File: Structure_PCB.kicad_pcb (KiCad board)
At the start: 2 copper layers, 180 x 100 mm, 101 parts, among them J10 JST-GH 4Pin, J11 JST-GH 4Pin, J12 JST-GH 4Pin, J6 6620XX236022_662004236022, J9 Conn_02x04_Top_Bottom, K2 FINDER-30.22

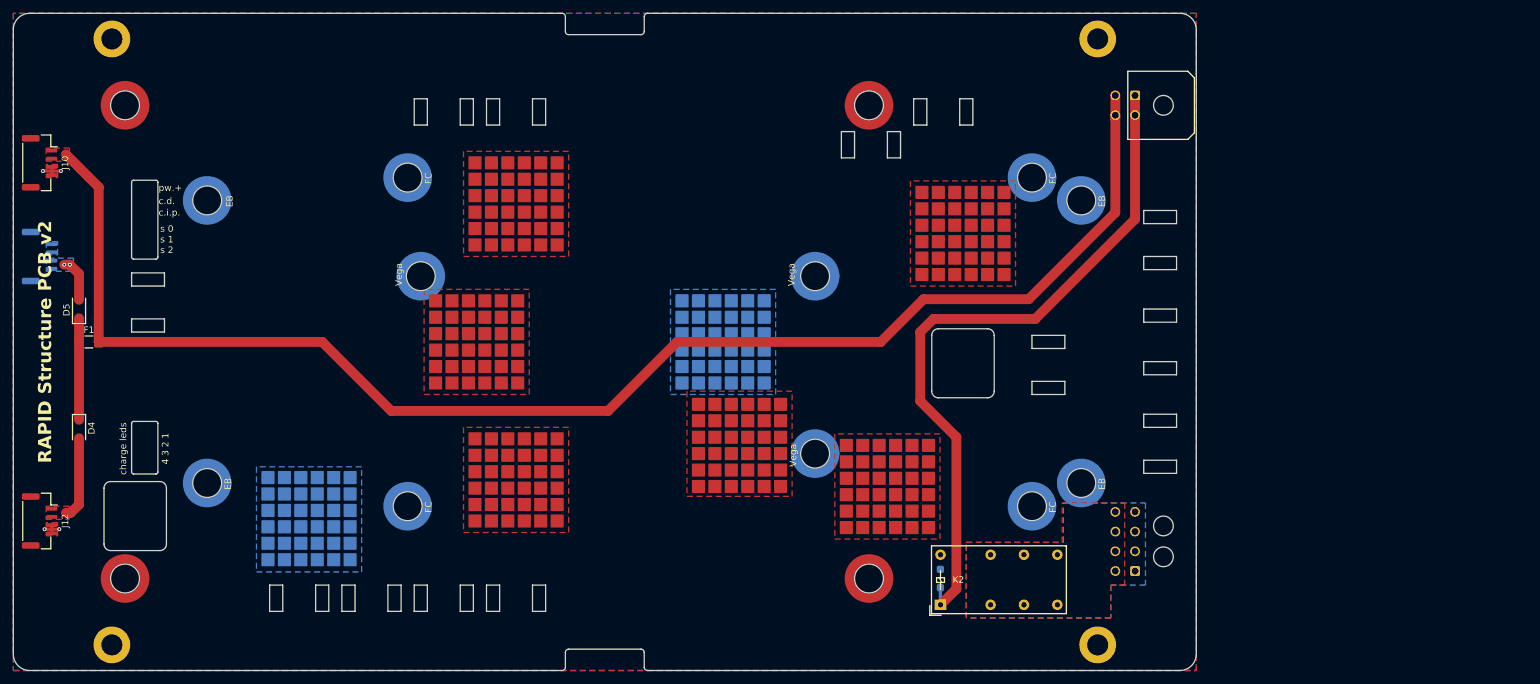
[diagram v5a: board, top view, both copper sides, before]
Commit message: added some thermal pads
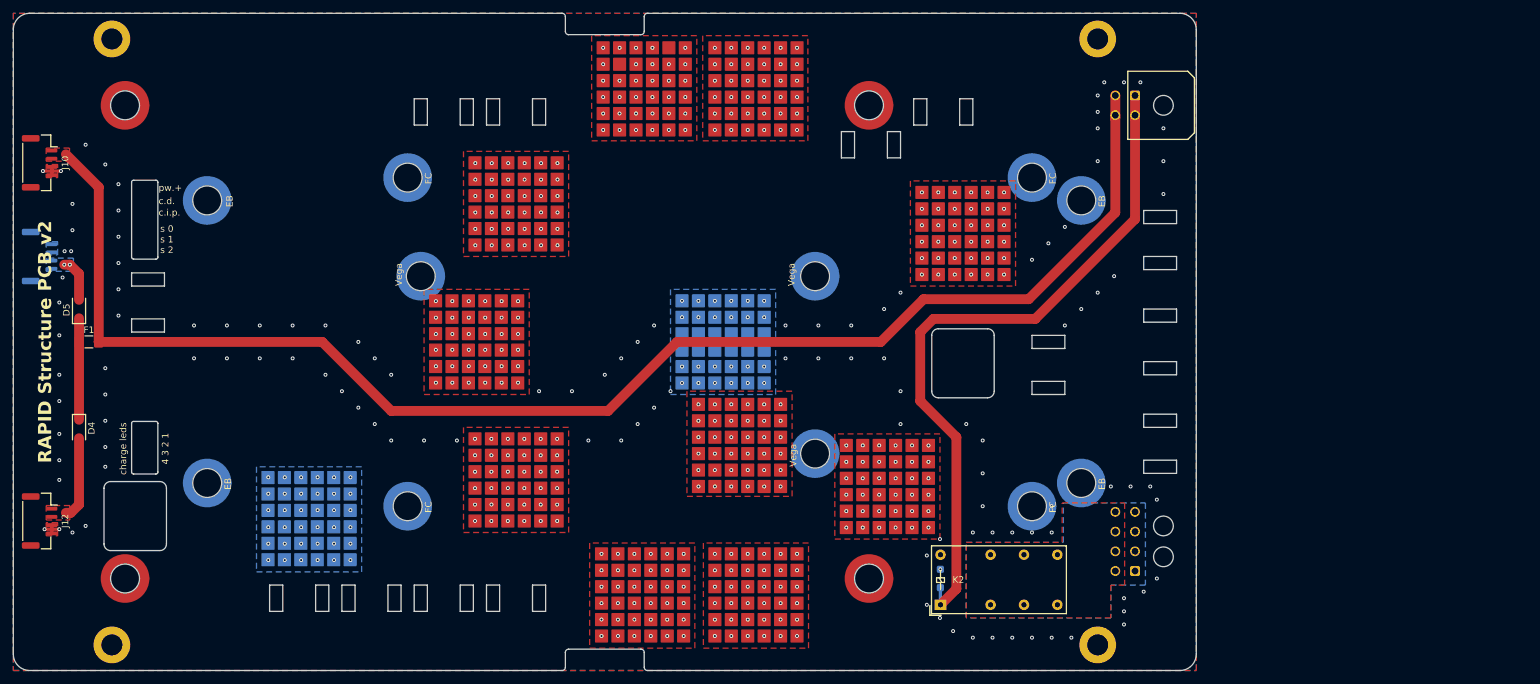
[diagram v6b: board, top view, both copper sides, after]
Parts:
- added HS100: Heatsink_Pad, Heatsink:würth 5x5 heat pads, F.Cu at (150.8, 138.5)
- added HS101: Heatsink_Pad, Heatsink:würth 5x5 heat pads, F.Cu at (168.0, 66.5)
- added HS102: Heatsink_Pad, Heatsink:würth 5x5 heat pads, F.Cu at (150.8, 143.5)
- added HS103: Heatsink_Pad, Heatsink:würth 5x5 heat pads, F.Cu at (141.0, 56.5)
- added HS104: Heatsink_Pad, Heatsink:würth 5x5 heat pads, F.Cu at (158.0, 133.5)
- added HS105: Heatsink_Pad, Heatsink:würth 5x5 heat pads, F.Cu at (141.0, 61.5)
- added HS106: Heatsink_Pad, Heatsink:würth 5x5 heat pads, F.Cu at (158.0, 138.5)
- added HS107: Heatsink_Pad, Heatsink:würth 5x5 heat pads, F.Cu at (141.0, 66.5)
- added HS108: Heatsink_Pad, Heatsink:würth 5x5 heat pads, F.Cu at (158.0, 143.5)
- added HS109: Heatsink_Pad, Heatsink:würth 5x5 heat pads, F.Cu at (146.0, 56.5)
- added HS110: Heatsink_Pad, Heatsink:würth 5x5 heat pads, F.Cu at (163.0, 133.5)
- added HS111: Heatsink_Pad, Heatsink:würth 5x5 heat pads, F.Cu at (146.0, 61.5)
- added HS112: Heatsink_Pad, Heatsink:würth 5x5 heat pads, F.Cu at (163.0, 138.5)
- added HS113: Heatsink_Pad, Heatsink:würth 5x5 heat pads, F.Cu at (146.0, 66.5)
- added HS114: Heatsink_Pad, Heatsink:würth 5x5 heat pads, F.Cu at (163.0, 143.5)
- added HS115: Heatsink_Pad, Heatsink:würth 5x5 heat pads, F.Cu at (151.0, 56.5)
- added HS116: Heatsink_Pad, Heatsink:würth 5x5 heat pads, F.Cu at (168.0, 133.5)
- added HS117: Heatsink_Pad, Heatsink:würth 5x5 heat pads, F.Cu at (151.0, 61.5)
- added HS118: Heatsink_Pad, Heatsink:würth 5x5 heat pads, F.Cu at (168.0, 138.5)
- added HS119: Heatsink_Pad, Heatsink:würth 5x5 heat pads, F.Cu at (151.0, 66.5)
- added HS120: Heatsink_Pad, Heatsink:würth 5x5 heat pads, F.Cu at (168.0, 143.5)
- added HS85: Heatsink_Pad, Heatsink:würth 5x5 heat pads, F.Cu at (158.0, 56.5)
- added HS86: Heatsink_Pad, Heatsink:würth 5x5 heat pads, F.Cu at (140.8, 133.5)
- added HS87: Heatsink_Pad, Heatsink:würth 5x5 heat pads, F.Cu at (158.0, 61.5)
- added HS88: Heatsink_Pad, Heatsink:würth 5x5 heat pads, F.Cu at (140.8, 138.5)
- added HS89: Heatsink_Pad, Heatsink:würth 5x5 heat pads, F.Cu at (158.0, 66.5)
- added HS90: Heatsink_Pad, Heatsink:würth 5x5 heat pads, F.Cu at (140.8, 143.5)
- added HS91: Heatsink_Pad, Heatsink:würth 5x5 heat pads, F.Cu at (163.0, 56.5)
- added HS92: Heatsink_Pad, Heatsink:würth 5x5 heat pads, F.Cu at (145.8, 133.5)
- added HS93: Heatsink_Pad, Heatsink:würth 5x5 heat pads, F.Cu at (163.0, 61.5)
- added HS94: Heatsink_Pad, Heatsink:würth 5x5 heat pads, F.Cu at (145.8, 138.5)
- added HS95: Heatsink_Pad, Heatsink:würth 5x5 heat pads, F.Cu at (163.0, 66.5)
- added HS96: Heatsink_Pad, Heatsink:würth 5x5 heat pads, F.Cu at (145.8, 143.5)
- added HS97: Heatsink_Pad, Heatsink:würth 5x5 heat pads, F.Cu at (168.0, 56.5)
- added HS98: Heatsink_Pad, Heatsink:würth 5x5 heat pads, F.Cu at (150.8, 133.5)
- added HS99: Heatsink_Pad, Heatsink:würth 5x5 heat pads, F.Cu at (168.0, 61.5)
- H1, H10, H11, H12, H13, H14, H15, H16, H17, H18, H19, H2, H3, H4, H5, H6, H7, H8, H9: value MountingHole -> MountingHole_Pad
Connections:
- H1 pad 1: (no net) -> GND
- H10 pad 1: (no net) -> GND
- H11 pad 1: (no net) -> GND
- H12 pad 1: (no net) -> GND
- H13 pad 1: (no net) -> GND
- H14 pad 1: (no net) -> GND
- H15 pad 1: (no net) -> GND
- H16 pad 1: (no net) -> GND
- H17 pad 1: (no net) -> GND
- H18 pad 1: (no net) -> GND
- H19 pad 1: (no net) -> GND
- H2 pad 1: (no net) -> GND
- H3 pad 1: (no net) -> GND
- H4 pad 1: (no net) -> GND
- H5 pad 1: (no net) -> GND
- H6 pad 1: (no net) -> GND
- H7 pad 1: (no net) -> GND
- H8 pad 1: (no net) -> GND
- H9 pad 1: (no net) -> GND
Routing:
- net GND: vias 4 -> 538

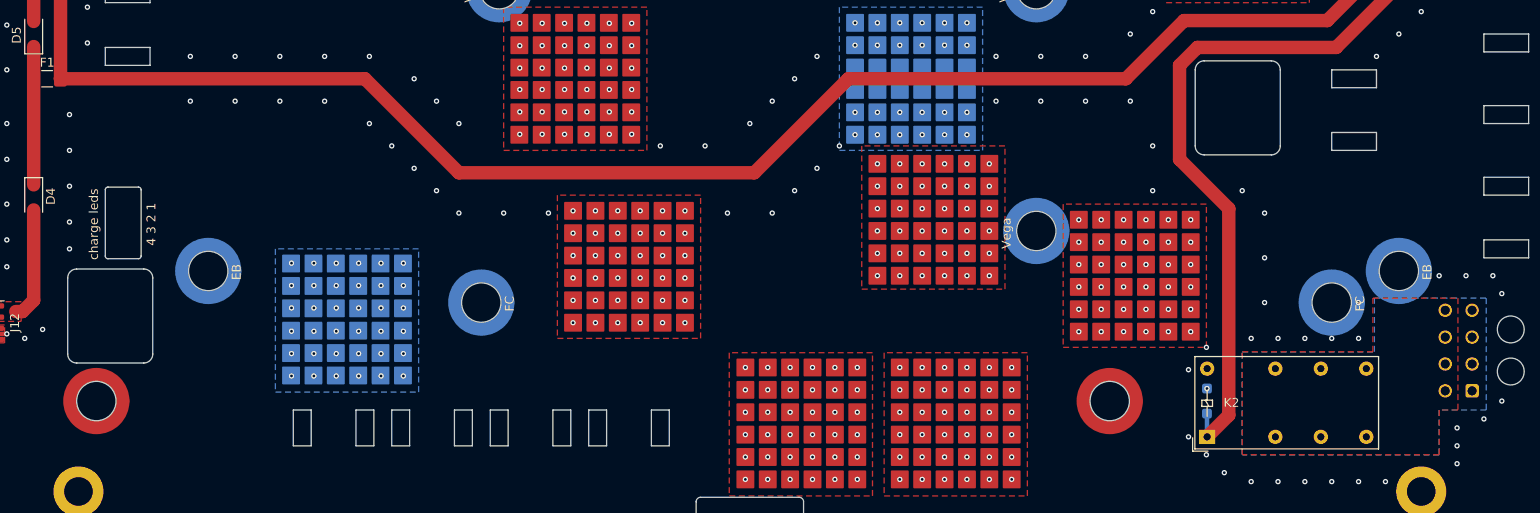
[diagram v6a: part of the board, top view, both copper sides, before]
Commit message: Fix relay footprint, correct zones, round off through trace
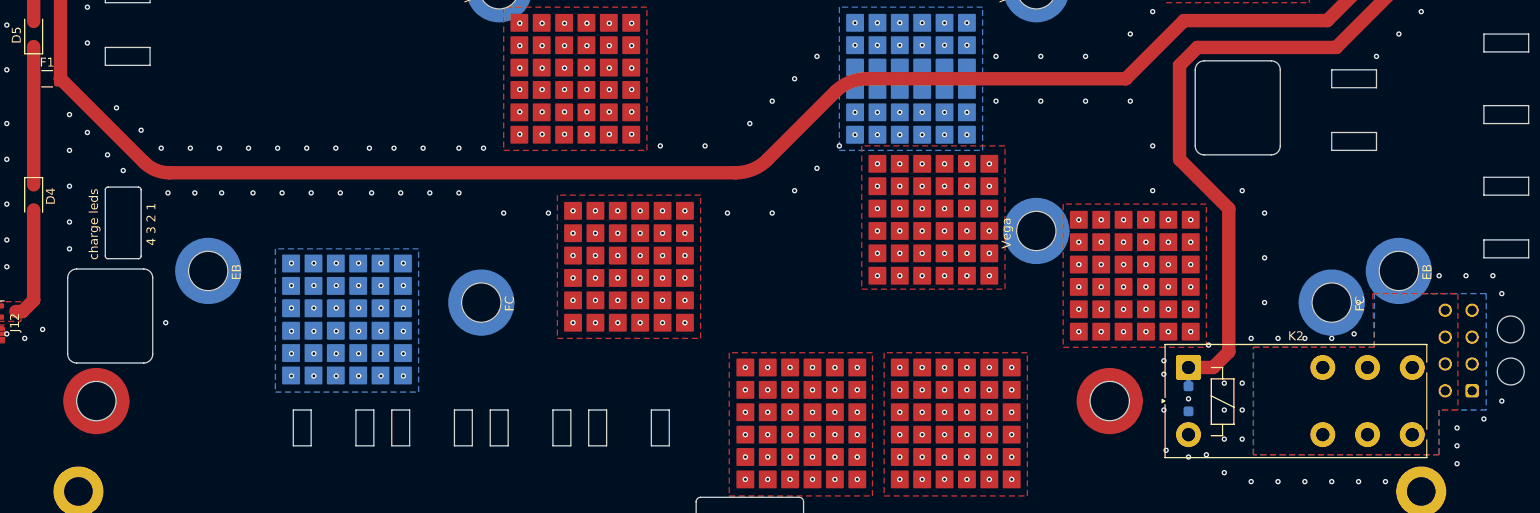
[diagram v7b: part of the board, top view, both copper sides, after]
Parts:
- K2: value FINDER-30.22 -> FINDER-40.61; footprint Relay_THT:Relay_DPDT_Finder_30.22 -> Relay_THT:Relay_SPDT_Finder_40.61
- moved K2 8.02 mm to (189.0, 132.2)
- moved D6 2.08 mm to (189.0, 135.8), turned to -90 degrees
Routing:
- net /post_arm: track 106.5 -> 100.7 mm
- net /SBout: track 220.5 -> 219.8 mm
- net GND: vias 538 -> 559

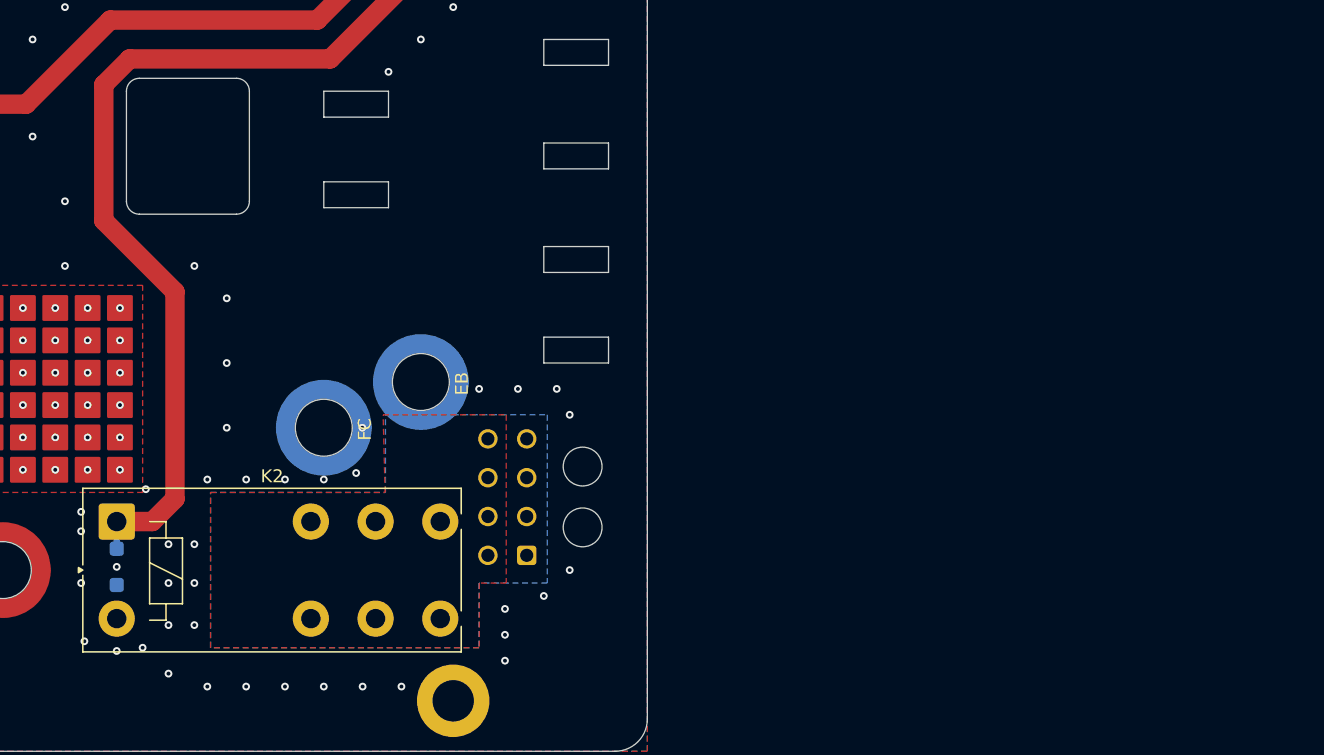
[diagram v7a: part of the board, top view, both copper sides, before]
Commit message: Increase distance between relais and fc
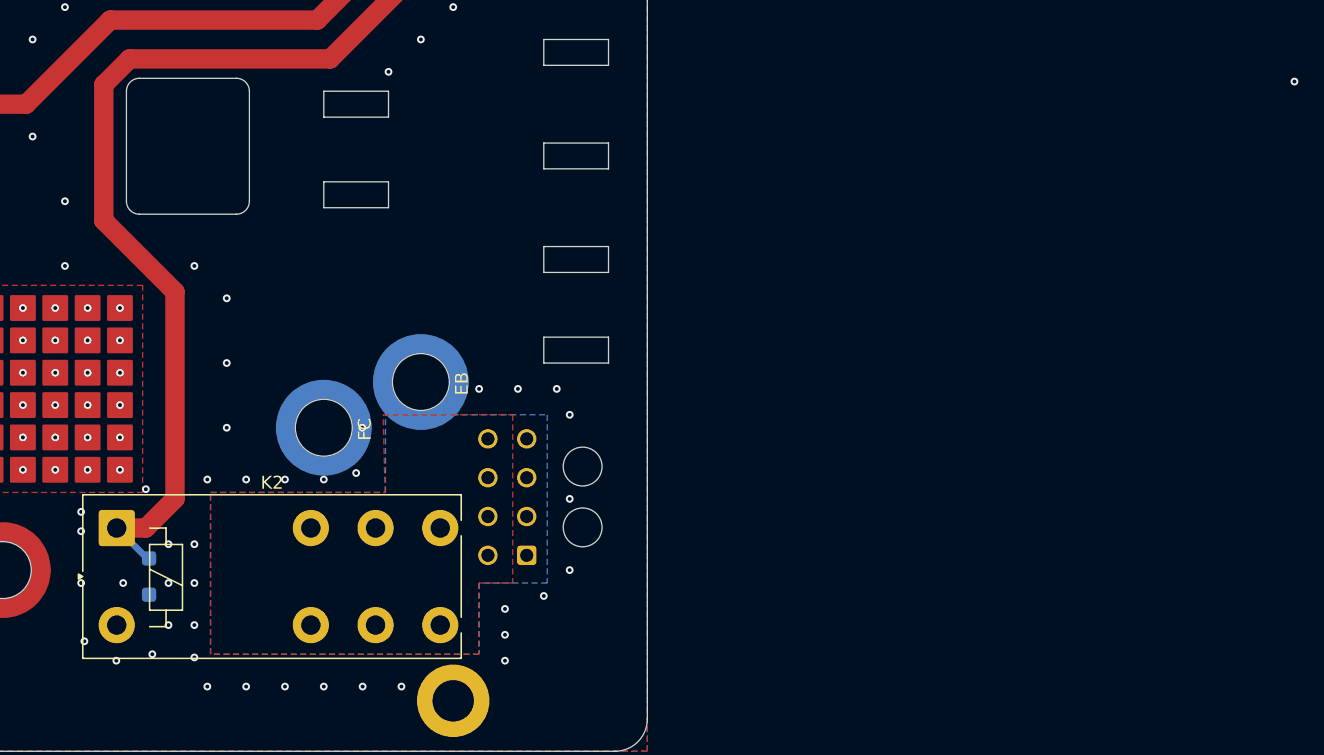
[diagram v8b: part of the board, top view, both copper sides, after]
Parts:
- moved D6 2.61 mm to (191.5, 136.5)
- moved K2 0.50 mm to (189.0, 132.8)
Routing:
- net /post_arm: track 100.7 -> 102.3 mm
- net GND: vias 559 -> 560
- net (no net): vias 0 -> 1
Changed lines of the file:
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@@
 	(footprint "Relay_THT:Relay_SPDT_Finder_40.61"
 		(layer "F.Cu")
-		(at 189 132.25)
+		(at 189 132.75)
 		(descr "SPDT relay, Finder 40.61, 16A, 250V, body size 29x12.4mm, height 25mm, pitch 5x7.5mm, https://cdn.findernet.com/app/uploads/S40EN.pdf")
 		(tags "2-Form-C")
@@
 	(footprint "Diode_SMD:D_SOD-123F"
 		(layer "B.Cu")
-		(at 189 135.75 -90)
+		(at 191.5 136.5 -90)
 		(descr "D_SOD-123F")
 		(tags "D_SOD-123F")
@@
 	)
 	(gr_text "PB power in"
-		(at 57.2 80 90)
+		(at 61 87 270)
 		(layer "B.Paste")
 		(effects
@@
 				(thickness 0.2)
 			)
-			(justify top)
+			(justify top mirror)
 		)
 	)
@@
 		)
 	)
+	(via
+		(at 280 98.25)
+		(size 0.6)
+		(drill 0.3)
+		(layers "F.Cu" "B.Cu")
+		(net 0)
+	)
 	(segment
 		(start 55.85 74)
@@
 	)
 	(via
-		(at 189 142.25)
+		(at 188.96785 143)
 		(size 0.6)
 		(drill 0.3)
@@
 	)
 	(via
-		(at 193 144)
+		(at 191.75 142.5)
 		(size 0.6)
 		(drill 0.3)
@@
 	)
 	(via
+		(at 224 130.5)
+		(size 0.6)
+		(drill 0.3)
+		(layers "F.Cu" "B.Cu")
+		(free yes)
+		(net 1)
+	)
+	(via
 		(at 124.3 93.8)
 		(size 0.6)
@@
 	)
 	(via
-		(at 191 142)
+		(at 195 142.75)
 		(size 0.6)
 		(drill 0.3)
@@
 	)
 	(via
-		(at 189 135.75)
+		(at 189.5 137)
 		(size 0.6)
 		(drill 0.3)
@@
 	)
 	(segment
-		(start 205.5 96.5)
-		(end 190 96.5)
+		(start 220.68 66)
+		(end 220.68 62.5)
 		(width 1.5)
 		(layer "F.Cu")
@@
 	)
 	(segment
-		(start 220.68 66)
-		(end 220.68 62.5)
+		(start 190 96.5)
+		(end 188 98.5)
 		(width 1.5)
 		(layer "F.Cu")
@@
 	)
 	(segment
-		(start 220.68 81.32)
-		(end 205.5 96.5)
+		(start 188 109)
+		(end 193.5 114.5)
 		(width 1.5)
 		(layer "F.Cu")
@@
 	)
 	(segment
-		(start 193.5 114.5)
-		(end 193.5 130.5)
+		(start 191.25 132.75)
+		(end 189 132.75)
 		(width 1.5)
 		(layer "F.Cu")
@@
 	)
 	(segment
-		(start 220.68 66)
-		(end 220.68 81.32)
+		(start 220.68 65.5)
+		(end 220.68 66)
 		(width 1.5)
 		(layer "F.Cu")
@@
 	)
 	(segment
-		(start 188 98.5)
-		(end 188 109)
+		(start 220.68 66)
+		(end 220.68 81.32)
 		(width 1.5)
 		(layer "F.Cu")
@@
 	)
 	(segment
-		(start 188 109)
-		(end 193.5 114.5)
+		(start 205.5 96.5)
+		(end 190 96.5)
 		(width 1.5)
 		(layer "F.Cu")
@@
 	)
 	(segment
-		(start 220.68 65.5)
-		(end 220.68 66)
+		(start 193.5 114.5)
+		(end 193.5 130.5)
 		(width 1.5)
 		(layer "F.Cu")
@@
 	)
 	(segment
-		(start 191.75 132.25)
-		(end 189 132.25)
+		(start 193.5 130.5)
+		(end 191.25 132.75)
 		(width 1.5)
 		(layer "F.Cu")
@@
 	)
 	(segment
-		(start 193.5 130.5)
-		(end 191.75 132.25)
+		(start 220.68 81.32)
+		(end 205.5 96.5)
 		(width 1.5)
 		(layer "F.Cu")
@@
 	)
 	(segment
-		(start 190 96.5)
-		(end 188 98.5)
+		(start 188 98.5)
+		(end 188 109)
 		(width 1.5)
 		(layer "F.Cu")
@@
 	)
 	(segment
-		(start 189 134.35)
-		(end 189 132.25)
+		(start 191.35 135.1)
+		(end 191.5 135.1)
+		(width 0.2)
+		(layer "B.Cu")
+		(net 7)
+	)
+	(segment
+		(start 189 132.75)
+		(end 191.35 135.1)
 		(width 0.5)
 		(layer "B.Cu")
@@
 		(polygon
 			(pts
-				(xy 196.25 130) (xy 209.737229 130) (xy 209.583975 124) (xy 219.096746 124) (xy 219.096746 137)
-				(xy 217 137) (xy 217 142) (xy 196.25 142)
+				(xy 196.25 130) (xy 209.737229 130) (xy 209.583975 124) (xy 219.596746 124) (xy 219.596746 137)
+				(xy 217 137) (xy 217 142.5) (xy 196.25 142.5)
 			)
 		)
@@
 			(pts
 				(xy 196.25 130) (xy 209.765 130) (xy 209.765 124) (xy 222.265 124) (xy 222.265 137) (xy 217 137)
-				(xy 217 142) (xy 196.25 142)
+				(xy 217 142.5) (xy 196.25 142.5)
 			)
 		)
